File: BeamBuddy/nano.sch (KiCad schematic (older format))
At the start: 12 parts, among them J10 ICSP, U3 MCU-ATMEGA328P-AU_TQFP32_, Y2 16MHZ

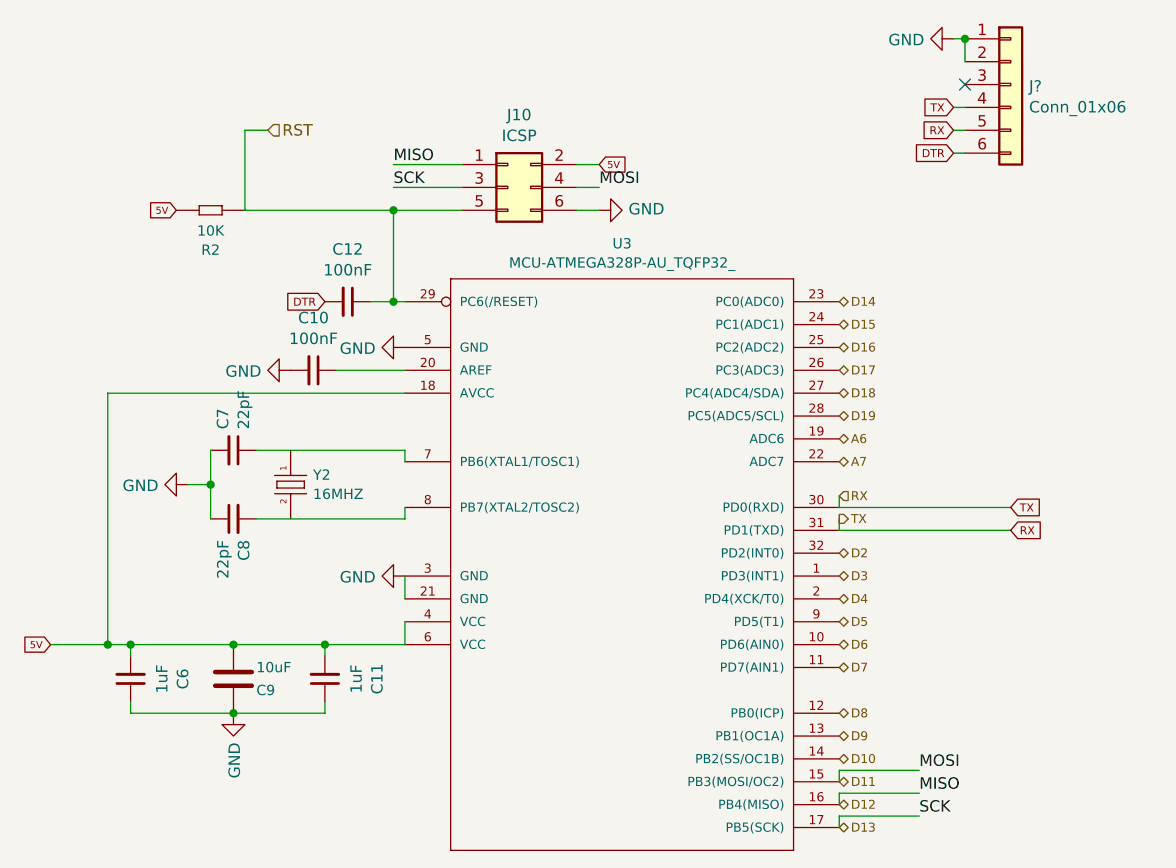
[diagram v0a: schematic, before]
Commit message: Added footprints
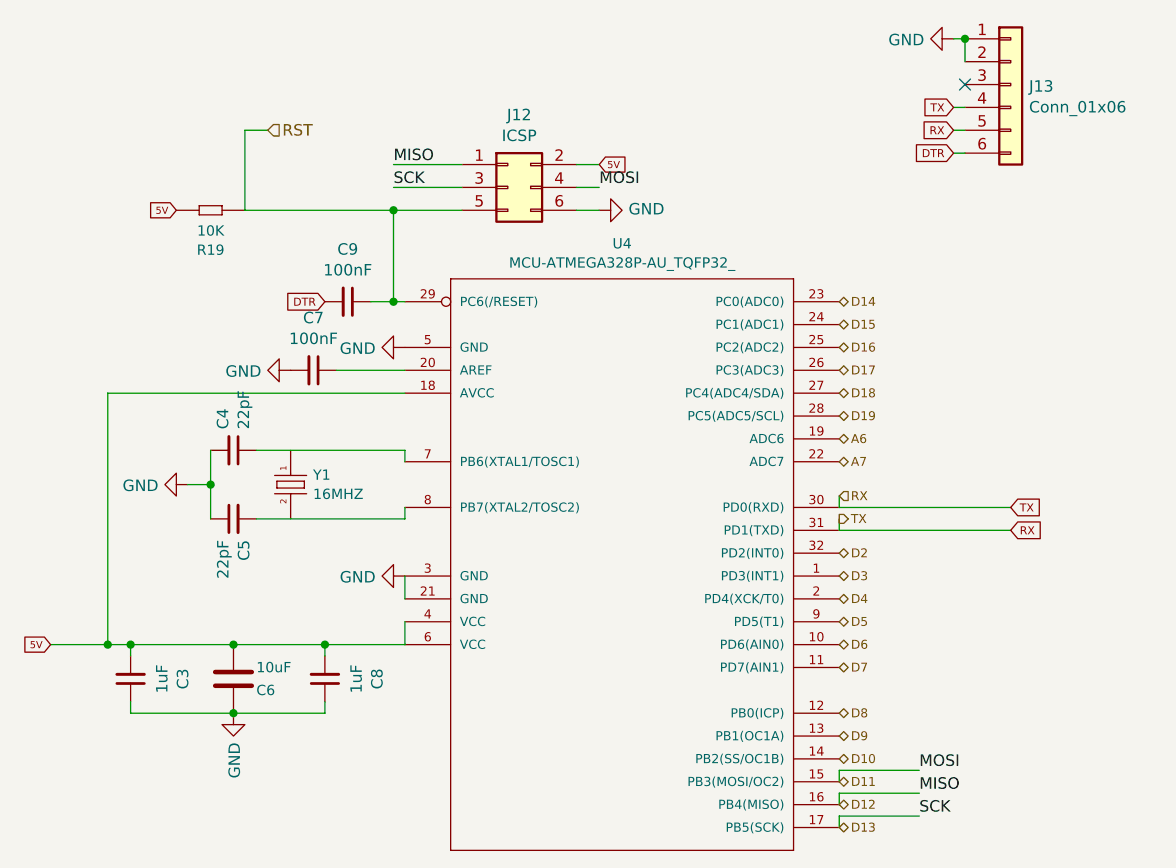
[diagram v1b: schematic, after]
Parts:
- J13: renamed from J?; footprint (none) -> Connector_PinHeader_2.54mm:PinHeader_1x06_P2.54mm_Vertical
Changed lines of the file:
@@
 AR Path="/5D499913/5D499CCE" Ref="U3"  Part="1"
 AR Path="/5D4AF8B7/5D499CCE" Ref="U?"  Part="1"
-AR Path="/5E7938E6/5D499CCE" Ref="U?"  Part="1"
-F 0 "U?" H 8450 4704 45  0000 C CNN
+AR Path="/5E7938E6/5D499CCE" Ref="U4"  Part="1"
+F 0 "U4" H 8450 4704 45  0000 C CNN
 F 1 "MCU-ATMEGA328P-AU_TQFP32_" H 8450 4620 45  0000 C CNN
 F 2 "OPL_Integrated_Circuit:TQFP32-0.8-7X7MM" H 8450 3300 50  0001 C CNN
@@
 AR Path="/5D499913/5D49BE16" Ref="Y2"  Part="1"
 AR Path="/5D4AF8B7/5D49BE16" Ref="Y?"  Part="1"
-AR Path="/5E7938E6/5D49BE16" Ref="Y?"  Part="1"
-F 0 "Y?" V 6958 3048 45  0000 L CNN
+AR Path="/5E7938E6/5D49BE16" Ref="Y1"  Part="1"
+F 0 "Y1" V 6958 3048 45  0000 L CNN
 F 1 "16MHZ" V 7042 3048 45  0000 L CNN
 F 2 "OPL_Crystal_Oscillator:X2-SMD-5.0X3.2X1.3MM" H 7000 2950 50  0001 C CNN
@@
 AR Path="/5D499913/5D49FB9B" Ref="#PWR016"  Part="1"
 AR Path="/5D4AF8B7/5D49FB9B" Ref="#PWR?"  Part="1"
-AR Path="/5E7938E6/5D49FB9B" Ref="#PWR?"  Part="1"
-F 0 "#PWR?" H 6550 2700 50  0001 C CNN
+AR Path="/5E7938E6/5D49FB9B" Ref="#PWR015"  Part="1"
+F 0 "#PWR015" H 6550 2700 50  0001 C CNN
 F 1 "GND" V 6555 2822 50  0000 R CNN
 F 2 "" H 6550 2950 50  0001 C CNN
@@
 AR Path="/5D499913/5D4D6BB8" Ref="#PWR020"  Part="1"
 AR Path="/5D4AF8B7/5D4D6BB8" Ref="#PWR?"  Part="1"
-AR Path="/5E7938E6/5D4D6BB8" Ref="#PWR?"  Part="1"
-F 0 "#PWR?" H 7500 2100 50  0001 C CNN
+AR Path="/5E7938E6/5D4D6BB8" Ref="#PWR018"  Part="1"
+F 0 "#PWR018" H 7500 2100 50  0001 C CNN
 F 1 "GND" V 7505 2222 50  0000 R CNN
 F 2 "" H 7500 2350 50  0001 C CNN
@@
 AR Path="/5D499913/5D4E4501" Ref="#PWR019"  Part="1"
 AR Path="/5D4AF8B7/5D4E4501" Ref="#PWR?"  Part="1"
-AR Path="/5E7938E6/5D4E4501" Ref="#PWR?"  Part="1"
-F 0 "#PWR?" H 7000 2200 50  0001 C CNN
+AR Path="/5E7938E6/5D4E4501" Ref="#PWR017"  Part="1"
+F 0 "#PWR017" H 7000 2200 50  0001 C CNN
 F 1 "GND" V 7005 2322 50  0000 R CNN
 F 2 "" H 7000 2450 50  0001 C CNN
@@
 AR Path="/5D499913/5D4E490D" Ref="#PWR021"  Part="1"
 AR Path="/5D4AF8B7/5D4E490D" Ref="#PWR?"  Part="1"
-AR Path="/5E7938E6/5D4E490D" Ref="#PWR?"  Part="1"
-F 0 "#PWR?" H 7500 3100 50  0001 C CNN
+AR Path="/5E7938E6/5D4E490D" Ref="#PWR019"  Part="1"
+F 0 "#PWR019" H 7500 3100 50  0001 C CNN
 F 1 "GND" V 7505 3222 50  0000 R CNN
 F 2 "" H 7500 3350 50  0001 C CNN
@@
 AR Path="/5D499913/5D4E5A8F" Ref="C11"  Part="1"
 AR Path="/5D4AF8B7/5D4E5A8F" Ref="C?"  Part="1"
-AR Path="/5E7938E6/5D4E5A8F" Ref="C?"  Part="1"
-F 0 "C?" V 6921 3800 50  0000 C CNN
+AR Path="/5E7938E6/5D4E5A8F" Ref="C8"  Part="1"
+F 0 "C8" V 6921 3800 50  0000 C CNN
 F 1 "1uF" V 7012 3800 50  0000 C CNN
 F 2 "OPL_Capacitor:C0603" H 7150 3800 50  0001 C CNN
@@
 AR Path="/5D499913/5D4E5FDE" Ref="C6"  Part="1"
 AR Path="/5D4AF8B7/5D4E5FDE" Ref="C?"  Part="1"
-AR Path="/5E7938E6/5D4E5FDE" Ref="C?"  Part="1"
-F 0 "C?" V 6071 3800 50  0000 C CNN
+AR Path="/5E7938E6/5D4E5FDE" Ref="C3"  Part="1"
+F 0 "C3" V 6071 3800 50  0000 C CNN
 F 1 "1uF" V 6162 3800 50  0000 C CNN
 F 2 "OPL_Capacitor:C0603" H 6300 3800 50  0001 C CNN
@@
 AR Path="/5D499913/5D4E7480" Ref="C9"  Part="1"
 AR Path="/5D4AF8B7/5D4E7480" Ref="C?"  Part="1"
-AR Path="/5E7938E6/5D4E7480" Ref="C?"  Part="1"
-F 0 "C?" H 6850 3750 45  0000 L CNN
+AR Path="/5E7938E6/5D4E7480" Ref="C6"  Part="1"
+F 0 "C6" H 6850 3750 45  0000 L CNN
 F 1 "10uF" H 6850 3850 45  0000 L CNN
 F 2 "OPL_Capacitor:C1206" H 6750 3800 50  0001 C CNN
@@
 AR Path="/5D499913/5D4EEC78" Ref="#PWR017"  Part="1"
 AR Path="/5D4AF8B7/5D4EEC78" Ref="#PWR?"  Part="1"
-AR Path="/5E7938E6/5D4EEC78" Ref="#PWR?"  Part="1"
-F 0 "#PWR?" H 6750 3700 50  0001 C CNN
+AR Path="/5E7938E6/5D4EEC78" Ref="#PWR016"  Part="1"
+F 0 "#PWR016" H 6750 3700 50  0001 C CNN
 F 1 "GND" V 6755 3822 50  0000 R CNN
 F 2 "" H 6750 3950 50  0001 C CNN
@@
 AR Path="/5D499913/5D4F1433" Ref="C8"  Part="1"
 AR Path="/5D4AF8B7/5D4F1433" Ref="C?"  Part="1"
-AR Path="/5E7938E6/5D4F1433" Ref="C?"  Part="1"
-F 0 "C?" H 6658 3054 50  0000 R CNN
+AR Path="/5E7938E6/5D4F1433" Ref="C5"  Part="1"
+F 0 "C5" H 6658 3054 50  0000 R CNN
 F 1 "22pF" H 6658 3145 50  0000 R CNN
 F 2 "OPL_Capacitor:C0603" H 6750 3100 50  0001 C CNN
@@
 AR Path="/5D499913/5D4F084E" Ref="C7"  Part="1"
 AR Path="/5D4AF8B7/5D4F084E" Ref="C?"  Part="1"
-AR Path="/5E7938E6/5D4F084E" Ref="C?"  Part="1"
-F 0 "C?" H 6658 2754 50  0000 R CNN
+AR Path="/5E7938E6/5D4F084E" Ref="C4"  Part="1"
+F 0 "C4" H 6658 2754 50  0000 R CNN
 F 1 "22pF" H 6658 2845 50  0000 R CNN
 F 2 "OPL_Capacitor:C0603" H 6750 2800 50  0001 C CNN
@@
 AR Path="/5D499913/5D4F2ACF" Ref="C12"  Part="1"
 AR Path="/5D4AF8B7/5D4F2ACF" Ref="C?"  Part="1"
-AR Path="/5E7938E6/5D4F2ACF" Ref="C?"  Part="1"
-F 0 "C?" V 7021 2150 50  0000 C CNN
+AR Path="/5E7938E6/5D4F2ACF" Ref="C9"  Part="1"
+F 0 "C9" V 7021 2150 50  0000 C CNN
 F 1 "100nF" V 7112 2150 50  0000 C CNN
 F 2 "OPL_Capacitor:C0805" H 7250 2150 50  0001 C CNN
@@
 AR Path="/5D499913/5D4F3261" Ref="C10"  Part="1"
 AR Path="/5D4AF8B7/5D4F3261" Ref="C?"  Part="1"
-AR Path="/5E7938E6/5D4F3261" Ref="C?"  Part="1"
-F 0 "C?" V 6871 2450 50  0000 C CNN
+AR Path="/5E7938E6/5D4F3261" Ref="C7"  Part="1"
+F 0 "C7" V 6871 2450 50  0000 C CNN
 F 1 "100nF" V 6962 2450 50  0000 C CNN
 F 2 "OPL_Capacitor:C0805" H 7100 2450 50  0001 C CNN
@@
 AR Path="/5D499913/5D502C92" Ref="J10"  Part="1"
 AR Path="/5D4AF8B7/5D502C92" Ref="J?"  Part="1"
-AR Path="/5E7938E6/5D502C92" Ref="J?"  Part="1"
-F 0 "J?" H 8000 1967 50  0000 C CNN
+AR Path="/5E7938E6/5D502C92" Ref="J12"  Part="1"
+F 0 "J12" H 8000 1967 50  0000 C CNN
 F 1 "ICSP" H 8000 1876 50  0000 C CNN
 F 2 "Connector_PinHeader_2.54mm:PinHeader_2x03_P2.54mm_Vertical" H 7950 1650 50  0001 C CNN
@@
 AR Path="/5D499913/5D50529E" Ref="#PWR022"  Part="1"
 AR Path="/5D4AF8B7/5D50529E" Ref="#PWR?"  Part="1"
-AR Path="/5E7938E6/5D50529E" Ref="#PWR?"  Part="1"
-F 0 "#PWR?" H 8350 1500 50  0001 C CNN
+AR Path="/5E7938E6/5D50529E" Ref="#PWR020"  Part="1"
+F 0 "#PWR020" H 8350 1500 50  0001 C CNN
 F 1 "GND" V 8355 1622 50  0000 R CNN
 F 2 "" H 8350 1750 50  0001 C CNN
@@
 AR Path="/5D499913/5D50C710" Ref="R2"  Part="1"
 AR Path="/5D4AF8B7/5D50C710" Ref="R?"  Part="1"
-AR Path="/5E7938E6/5D50C710" Ref="R?"  Part="1"
-F 0 "R?" H 6650 1924 45  0000 C CNN
+AR Path="/5E7938E6/5D50C710" Ref="R19"  Part="1"
+F 0 "R19" H 6650 1924 45  0000 C CNN
 F 1 "10K" H 6650 1840 45  0000 C CNN
 F 2 "OPL_Resistor:R0603" H 6650 1750 40  0001 C CNN
@@
 	9400 3150 10150 3150
 $Comp
-L Connector_Generic:Conn_01x06 J?
+L Connector_Generic:Conn_01x06 J13
 U 1 1 5E798A81
 P 10150 1200
-F 0 "J?" H 10230 1192 50  0000 L CNN
+F 0 "J13" H 10230 1192 50  0000 L CNN
 F 1 "Conn_01x06" H 10230 1101 50  0000 L CNN
-F 2 "" H 10150 1200 50  0001 C CNN
+F 2 "Connector_PinHeader_2.54mm:PinHeader_1x06_P2.54mm_Vertical" H 10150 1200 50  0001 C CNN
 F 3 "~" H 10150 1200 50  0001 C CNN
 	1    10150 1200
@@
 AR Path="/5D499913/5E79F8A6" Ref="#PWR?"  Part="1"
 AR Path="/5D4AF8B7/5E79F8A6" Ref="#PWR?"  Part="1"
-AR Path="/5E7938E6/5E79F8A6" Ref="#PWR?"  Part="1"
-F 0 "#PWR?" H 9900 750 50  0001 C CNN
+AR Path="/5E7938E6/5E79F8A6" Ref="#PWR021"  Part="1"
+F 0 "#PWR021" H 9900 750 50  0001 C CNN
 F 1 "GND" V 9905 872 50  0000 R CNN
 F 2 "" H 9900 1000 50  0001 C CNN

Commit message: Finished proto PCB
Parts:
- C9: MPN CC1206KKX5R8BB106 -> 1276-6736-1-ND; SKU 302010181 -> 1276-6736-1-ND
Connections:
- net RX: no longer J13.4 (Pin_4), U3.30 (PD0(RXD))
- net at C7.1, U3.7 (PB6(XTAL1/TOSC1)): now also Y2.1
- net at C8.2, U3.8 (PB7(XTAL2/TOSC2)): now also Y2.2
- new net TX: J13.4 (Pin_4), U3.30 (PD0(RXD))
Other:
- moved on the sheet: J13
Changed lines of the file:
@@
 F 2 "OPL_Capacitor:C1206" H 6750 3800 50  0001 C CNN
 F 3 "" H 6750 3800 50  0001 C CNN
-F 4 "CC1206KKX5R8BB106" H 6780 3950 20  0001 C CNN "MPN"
-F 5 "302010181" H 6780 3950 20  0001 C CNN "SKU"
+F 4 "1276-6736-1-ND" H 6780 3950 20  0001 C CNN "MPN"
+F 5 "1276-6736-1-ND" H 6780 3950 20  0001 C CNN "SKU"
 	1    6750 3800
 	1    0    0    -1
@@
 Text GLabel 5950 3650 0    31   Input ~ 0
 5V
-Text HLabel 9400 3100 2    39   Output ~ 0
-TX
-Text HLabel 9400 3000 2    39   Input ~ 0
-RX
-Wire Wire Line
-	9400 3100 9400 3150
-Wire Wire Line
-	9400 3000 9400 3050
 Text HLabel 6900 1400 2    50   Input ~ 0
 RST
@@
 	6750 3650 7150 3650
 Wire Wire Line
-	6850 2800 7500 2800
-Wire Wire Line
-	6850 3100 7500 3100
-Wire Wire Line
-	9400 3050 10150 3050
-Wire Wire Line
-	9400 3150 10150 3150
+	6850 2800 7000 2800
+Wire Wire Line
+	6850 3100 7000 3100
 $Comp
 L Connector_Generic:Conn_01x06 J13
 U 1 1 5E798A81
-P 10150 1200
-F 0 "J13" H 10230 1192 50  0000 L CNN
-F 1 "Conn_01x06" H 10230 1101 50  0000 L CNN
-F 2 "Connector_PinHeader_2.54mm:PinHeader_1x06_P2.54mm_Vertical" H 10150 1200 50  0001 C CNN
-F 3 "~" H 10150 1200 50  0001 C CNN
-	1    10150 1200
+P 10200 2950
+F 0 "J13" H 10280 2942 50  0000 L CNN
+F 1 "Conn_01x06" H 10280 2851 50  0000 L CNN
+F 2 "Connector_PinHeader_2.54mm:PinHeader_1x06_P2.54mm_Vertical" H 10200 2950 50  0001 C CNN
+F 3 "~" H 10200 2950 50  0001 C CNN
+	1    10200 2950
 	1    0    0    -1
 $EndComp
-Text GLabel 9900 1300 0    35   Input ~ 0
-TX
-Text GLabel 9900 1400 0    35   Input ~ 0
-RX
-Text GLabel 9900 1500 0    35   Input ~ 0
+Text GLabel 9950 3250 0    35   Input ~ 0
 DTR
 Wire Wire Line
-	9900 1000 9950 1000
-Wire Wire Line
-	9950 1100 9950 1000
-Connection ~ 9950 1000
-Wire Wire Line
-	9900 1300 9950 1300
-Wire Wire Line
-	9900 1400 9950 1400
-Wire Wire Line
-	9900 1500 9950 1500
+	9950 2750 10000 2750
+Wire Wire Line
+	10000 2850 10000 2750
+Connection ~ 10000 2750
+Wire Wire Line
+	9950 3250 10000 3250
 $Comp
 L power:GND #PWR?
 U 1 1 5E79F8A6
-P 9900 1000
+P 9950 2750
 AR Path="/5D499913/5E79F8A6" Ref="#PWR?"  Part="1"
 AR Path="/5D4AF8B7/5E79F8A6" Ref="#PWR?"  Part="1"
 AR Path="/5E7938E6/5E79F8A6" Ref="#PWR021"  Part="1"
-F 0 "#PWR021" H 9900 750 50  0001 C CNN
-F 1 "GND" V 9905 872 50  0000 R CNN
-F 2 "" H 9900 1000 50  0001 C CNN
-F 3 "" H 9900 1000 50  0001 C CNN
-	1    9900 1000
+F 0 "#PWR021" H 9950 2500 50  0001 C CNN
+F 1 "GND" V 9955 2622 50  0000 R CNN
+F 2 "" H 9950 2750 50  0001 C CNN
+F 3 "" H 9950 2750 50  0001 C CNN
+	1    9950 2750
 	0    1    1    0
 $EndComp
-Text GLabel 10150 3150 2    35   Input ~ 0
-RX
-Text GLabel 10150 3050 2    35   Input ~ 0
-TX
 Text GLabel 7150 2150 0    35   Input ~ 0
 DTR
-NoConn ~ 9950 1200
+NoConn ~ 10000 2950
+Connection ~ 7000 2800
+Wire Wire Line
+	7000 2800 7500 2800
+Connection ~ 7000 3100
+Wire Wire Line
+	7000 3100 7500 3100
+Wire Wire Line
+	9400 3050 10000 3050
+Wire Wire Line
+	9400 3150 10000 3150
+Text Label 9750 3050 0    50   ~ 0
+TX
+Text Label 9750 3150 0    50   ~ 0
+RX
 $EndSCHEMATC

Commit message: Now with full DigiKey PNs
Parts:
- C10, C12: DK_PN (none) -> 311-1140-1-ND; Field5 CC0805KRX7R9BB104 -> (none); MPN (none) -> CC0805KRX7R9BB104
- C11: DK_PN (none) -> 311-1802-1-ND; MPN (none) -> CC0603KRX7R8BB105
- C6: DK_PN (none) -> 311-1802-1-ND
- C7, C8: DK_PN (none) -> 311-1062-1-ND
- C9: DK_PN (none) -> 1276-6736-1-ND; MPN 1276-6736-1-ND -> CL31A106MBHNNNE; SKU 1276-6736-1-ND -> (none)
- R2: DK_PN (none) -> 311-10.0KHRCT-ND; SKU 301010299 -> (none)
- Y2: DK_PN (none) -> 535-9103-1-ND; MPN X053201602002 -> ABM3-16.000MHZ-B2-T; SKU 306010054 -> (none)
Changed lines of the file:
@@
 F 2 "OPL_Crystal_Oscillator:X2-SMD-5.0X3.2X1.3MM" H 7000 2950 50  0001 C CNN
 F 3 "" H 7000 2950 50  0001 C CNN
-F 4 "X053201602002" H 7030 3100 20  0001 C CNN "MPN"
-F 5 "306010054" H 7030 3100 20  0001 C CNN "SKU"
+F 4 "ABM3-16.000MHZ-B2-T" H 7030 3100 20  0001 C CNN "MPN"
+F 5 "535-9103-1-ND" H 7030 3100 20  0001 C CNN "DK_PN"
 	1    7000 2950
 	0    1    1    0
@@
 F 3 "~" H 7150 3800 50  0001 C CNN
 F 4 "302010139" H 7150 3800 50  0001 C CNN "SKU"
-F 5 "" H 7150 3800 50  0001 C CNN "Field5"
+F 5 "CC0603KRX7R8BB105" H 7150 3800 50  0001 C CNN "MPN"
+F 6 "311-1802-1-ND" V 7150 3800 50  0001 C CNN "DK_PN"
 	1    7150 3800
 	-1   0    0    1
@@
 F 4 "302010139" H 6300 3800 50  0001 C CNN "SKU"
 F 5 "CC0603KRX7R8BB105" H 6300 3800 50  0001 C CNN "MPN"
+F 6 "311-1802-1-ND" V 6300 3800 50  0001 C CNN "DK_PN"
 	1    6300 3800
 	-1   0    0    1
@@
 F 2 "OPL_Capacitor:C1206" H 6750 3800 50  0001 C CNN
 F 3 "" H 6750 3800 50  0001 C CNN
-F 4 "1276-6736-1-ND" H 6780 3950 20  0001 C CNN "MPN"
-F 5 "1276-6736-1-ND" H 6780 3950 20  0001 C CNN "SKU"
+F 4 "CL31A106MBHNNNE" H 6780 3950 20  0001 C CNN "MPN"
+F 5 "1276-6736-1-ND" H 6780 3950 20  0001 C CNN "DK_PN"
 	1    6750 3800
 	1    0    0    -1
@@
 F 4 "302010143" H 6750 3100 50  0001 C CNN "SKU"
 F 5 "CC0603JRNPO9BN220" H 6750 3100 50  0001 C CNN "MPN"
+F 6 "311-1062-1-ND" H 6750 3100 50  0001 C CNN "DK_PN"
 	1    6750 3100
 	0    -1   -1   0
@@
 F 4 "302010143" H 6750 2800 50  0001 C CNN "SKU"
 F 5 "CC0603JRNPO9BN220" H 6750 2800 50  0001 C CNN "MPN"
+F 6 "311-1062-1-ND" H 6750 2800 50  0001 C CNN "DK_PN"
 	1    6750 2800
 	0    1    1    0
@@
 F 3 "~" H 7250 2150 50  0001 C CNN
 F 4 "302010165" H 7250 2150 50  0001 C CNN "SKU"
-F 5 "CC0805KRX7R9BB104" H 7250 2150 50  0001 C CNN "Field5"
+F 5 "CC0805KRX7R9BB104" H 7250 2150 50  0001 C CNN "MPN"
+F 6 "311-1140-1-ND" V 7250 2150 50  0001 C CNN "DK_PN"
 	1    7250 2150
 	0    1    1    0
@@
 F 3 "~" H 7100 2450 50  0001 C CNN
 F 4 "302010165" H 7100 2450 50  0001 C CNN "SKU"
-F 5 "CC0805KRX7R9BB104" H 7100 2450 50  0001 C CNN "Field5"
+F 5 "CC0805KRX7R9BB104" H 7100 2450 50  0001 C CNN "MPN"
+F 6 "311-1140-1-ND" V 7100 2450 50  0001 C CNN "DK_PN"
 	1    7100 2450
 	0    1    1    0
@@
 F 3 "" H 6650 1750 40  0001 C CNN
 F 4 "RC0603FR-0710KL" H 6680 1900 20  0001 C CNN "MPN"
-F 5 "301010299" H 6680 1900 20  0001 C CNN "SKU"
+F 5 "311-10.0KHRCT-ND" H 6680 1900 20  0001 C CNN "DK_PN"
 	1    6650 1750
 	-1   0    0    1
